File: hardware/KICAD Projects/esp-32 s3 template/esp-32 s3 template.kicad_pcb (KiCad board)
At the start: 2 copper layers, 55.5 x 39.5 mm, 28 parts, among them J1 TYPE-C-31-M-12, J2 TFTLCDS2, SW1 PTS810_SJM_250_SMTR_LFS, SW2 PTS810_SJM_250_SMTR_LFS, U1 AMS1117-3.3, U2 ESP32-S3-WROOM-1

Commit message: started the can integration
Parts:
- moved SW1 78.1 mm to (81.8, 71.6)
- moved SW2 77.8 mm to (81.8, 78.0)
- moved D6 76.4 mm to (79.6, 64.5), turned to 90 degrees
- moved C9 60.7 mm to (77.8, 71.7), turned to 90 degrees
- moved C10 59.5 mm to (77.7, 78.1), turned to 90 degrees
- moved R5 57.2 mm to (85.6, 71.5), turned to -90 degrees
- moved R4 56.7 mm to (87.0, 66.7), turned to 90 degrees
- moved C8 56.7 mm to (84.8, 63.1), turned to 90 degrees
- moved C6 56.7 mm to (84.8, 66.7), turned to -90 degrees
- moved R6 55.7 mm to (85.8, 77.9), turned to -90 degrees
- moved D3 54.5 mm to (110.2, 77.5)
- moved D2 54.4 mm to (110.3, 74.7)
- moved D4 54.4 mm to (110.2, 80.3)
- moved C7 53.6 mm to (87.0, 63.1), turned to 90 degrees
- moved D1 49.7 mm to (115.5, 70.0)
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
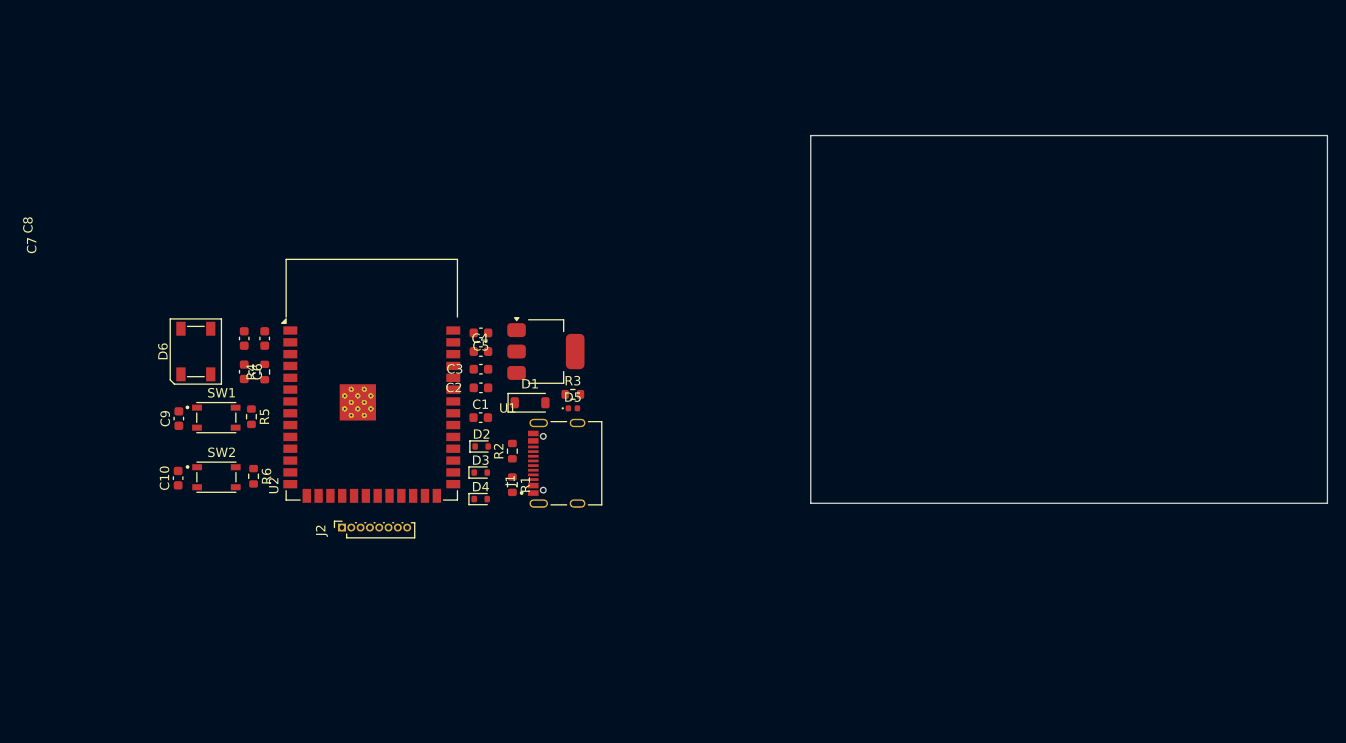
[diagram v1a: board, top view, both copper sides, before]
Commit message: finished pcb component layout for smd temp sense
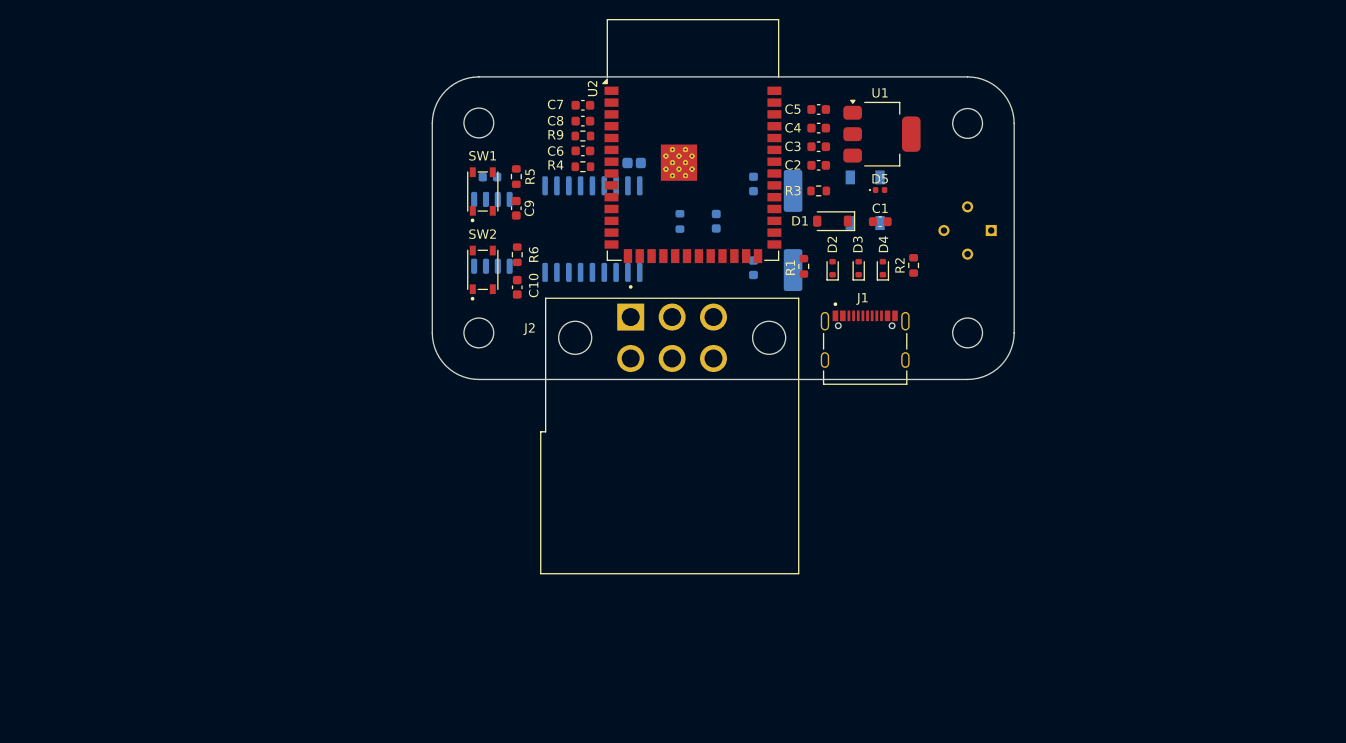
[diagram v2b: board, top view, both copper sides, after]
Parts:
- added C11: 10uF/16V, Capacitor_Tantalum_SMD:CP_EIA-1608-08_AVX-J, B.Cu at (126.7, 44.2)
- added C12: 100nF, Capacitor_SMD:C_0603_1608Metric, B.Cu at (135.5, 50.5)
- added C13: 22pF, Capacitor_SMD:C_0603_1608Metric, B.Cu at (139.5, 46.5)
- added C14: 22pF, Capacitor_SMD:C_0603_1608Metric, B.Cu at (139.5, 55.5)
- added C15: 100nF, Capacitor_SMD:C_0603_1608Metric, B.Cu at (111.2, 45.8)
- added R8: 10kΩ, Resistor_SMD:R_0603_1608Metric, B.Cu at (131.6, 50.5)
- added R9: 10k, Resistor_SMD:R_0603_1608Metric, F.Cu at (121.2, 41.4)
- added REF**: MountingHole_3.2mm_M3, MountingHole:MountingHole_3.2mm_M3, F.Cu at (110.0, 40.0)
- added REF**: MountingHole_3.2mm_M3, MountingHole:MountingHole_3.2mm_M3, F.Cu at (162.5, 62.5)
- added REF**: MountingHole_3.2mm_M3, MountingHole:MountingHole_3.2mm_M3, F.Cu at (162.5, 40.0)
- added REF**: MountingHole_3.2mm_M3, MountingHole:MountingHole_3.2mm_M3, F.Cu at (110.0, 62.5)
- added U3: MCP2515-I, Package_SO:SOIC-18W_7.5x11.6mm_P1.27mm, B.Cu at (122.2, 51.4)
- added U4: TJA1050DRG, Package_SO:SOIC-8_5.3x5.3mm_P1.27mm, B.Cu at (111.4, 51.8)
- added U5: ~, 0_Custom:MLX90614, B.Cu at (162.5, 51.5)
- added X1: 8MHz, Crystal:Crystal_SMD_HC49-SD, B.Cu at (143.8, 51.5)
- D6: moved to B.Cu
- J2: value TFTLCDS2 -> DTF13-6P; footprint Connector_PinSocket_1.00mm:PinSocket_1x08_P1.00mm_Vertical -> 0_Custom:TE_DTF13-6P
- moved D6 73.7 mm to (151.5, 48.2)
- moved D4 49.8 mm to (153.4, 55.5), turned to 90 degrees
- moved C1 47.8 mm to (153.1, 50.5)
- moved R2 47.5 mm to (156.7, 55.2)
- moved D3 46.2 mm to (150.8, 55.5), turned to 90 degrees
- moved C4 43.5 mm to (146.5, 40.5)
- moved C5 43.5 mm to (146.5, 38.5)
- moved C2 43.4 mm to (146.5, 44.5)
- moved C3 43.4 mm to (146.5, 42.5)
- moved C6 43.4 mm to (121.2, 43.0), turned to 180 degrees
- moved C8 43.2 mm to (121.2, 39.8), turned to 180 degrees
- moved U2 43.1 mm to (133.0, 41.8)
- moved U1 43.0 mm to (153.3, 41.1)
- moved C9 42.7 mm to (114.0, 49.1), turned to -90 degrees
- moved C7 42.4 mm to (121.2, 38.0), turned to 180 degrees
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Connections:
- C4 pad 1: ESP_3V3 -> VCC_3V3
- C5 pad 1: ESP_3V3 -> VCC_3V3
- C7 pad 1: ESP_3V3 -> VCC_3V3
- C8 pad 1: ESP_3V3 -> VCC_3V3
- D6 pad 3: ESP_3V3 -> VCC_3V3
- J2 pad 1: ESP_3V3 -> VCC_5V
- J2 pad 3: DIN -> Low
- J2 pad 4: CLK -> High
- J2 pad 5: CS -> Low
- J2 pad 6: DC -> High
- R3 pad 1: ESP_3V3 -> VCC_3V3
- R5 pad 1: ESP_3V3 -> VCC_3V3
- R6 pad 1: ESP_3V3 -> VCC_3V3
- U1 pad 2: ESP_3V3 -> VCC_3V3
- U2 pad 16: unconnected-(U2-IO46-Pad16) -> SCL
- U2 pad 2: ESP_3V3 -> VCC_3V3
- U2 pad 24: unconnected-(U2-IO47-Pad24) -> SO
- U2 pad 25: unconnected-(U2-IO48-Pad25) -> SI
- U2 pad 26: unconnected-(U2-IO45-Pad26) -> SDA
- U2 pad 38: unconnected-(U2-IO2-Pad38) -> VCC_3V3
- U2 pad 6: unconnected-(U2-IO6-Pad6) -> SCK
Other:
- board size 55.5 x 39.5 mm -> 62.5 x 32.5 mm

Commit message: everything but the ground fill
done, having some trouble with the ground fills
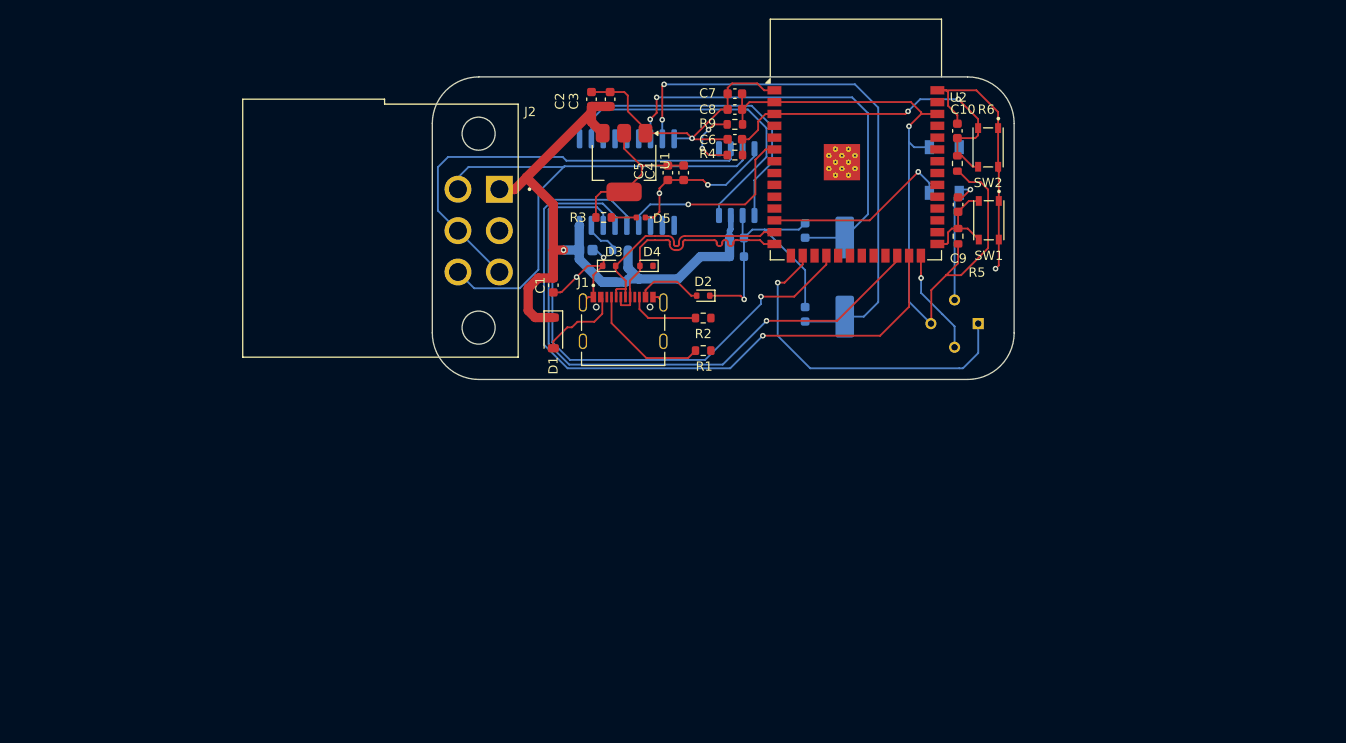
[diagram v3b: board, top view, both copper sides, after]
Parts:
- removed REF** (x4): MountingHole_3.2mm_M3, MountingHole:MountingHole_3.2mm_M3
- moved SW2 55.8 mm to (164.7, 42.6), turned to -90 degrees
- moved SW1 54.4 mm to (164.8, 50.4), turned to -90 degrees
- moved C10 50.2 mm to (161.4, 40.8), turned to 90 degrees
- moved R6 48.3 mm to (161.4, 44.3)
- moved R5 47.9 mm to (161.5, 52.1)
- moved C9 47.5 mm to (161.5, 48.7), turned to 90 degrees
- moved C1 35.8 mm to (118.0, 57.4), turned to -90 degrees
- moved D1 32.3 mm to (118.0, 62.5), turned to -90 degrees
- moved U1 27.9 mm to (125.6, 44.2), turned to -90 degrees
- moved C15 27.3 mm to (137.7, 52.3), turned to 180 degrees
- moved U4 26.9 mm to (137.7, 46.3), turned to 90 degrees
- moved D3 26.8 mm to (124.0, 55.3), turned to 0 degrees
- moved J1 26.1 mm to (125.5, 63.4)
- moved D5 25.9 mm to (127.4, 50.1), turned to 180 degrees
- moved C2 25.4 mm to (122.1, 37.4), turned to 90 degrees
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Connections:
- U2 pad 12: DIN -> RGB
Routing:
- net GND: track 0.00 -> 140.1 mm, vias 0 -> 8
- net VCC_3V3: track 0.00 -> 95.5 mm, vias 0 -> 1
- net VCC_5V: track 0.00 -> 74.3 mm, vias 0 -> 1
- net SI: track 0.00 -> 74.1 mm, vias 0 -> 1
- net SO: track 0.00 -> 66.9 mm, vias 0 -> 1
- net Net-(U3-OSC1): track 0.00 -> 59.6 mm, vias 0 -> 2
- net CS: track 0.00 -> 57.2 mm, vias 0 -> 1
- net High: track 0.00 -> 56.3 mm
- net Low: track 0.00 -> 47.3 mm
- net Net-(U3-OSC2): track 0.00 -> 46.8 mm, vias 0 -> 2
- net CHIP_PU: track 0.00 -> 39.0 mm, vias 0 -> 2
- net SCL: track 0.00 -> 37.0 mm, vias 0 -> 1
- net Net-(U3-TXCAN): track 0.00 -> 34.7 mm
- net Net-(U3-RXCAN): track 0.00 -> 33.6 mm
- net D+: track 0.00 -> 26.3 mm
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
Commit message: Finished it
Figured out zone fills
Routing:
- added copper zone on B.Cu, net GND
- added copper zone on F.Cu, net GND
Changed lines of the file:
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@@
 		(net 58)
+	)
+	(zone
+		(net 2)
+		(net_name "GND")
+		(layers "F.Cu" "B.Cu")
+		(hatch edge 0.5)
+		(connect_pads
+			(clearance 0.5)
+		)
+		(min_thickness 0.25)
+		(filled_areas_thickness no)
+		(fill yes
+			(thermal_gap 0.5)
+			(thermal_bridge_width 0.5)
+		)
+		(polygon
+			(pts
+				(xy 110 35) (xy 105 40) (xy 105 63) (xy 110 67.5) (xy 162 67.5) (xy 167.5 62) (xy 167.5 40) (xy 162 35)
+			)
+		)
 	)
 	(generated

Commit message: nfkljasdnfl
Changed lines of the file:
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@@
 			(outputformat 1)
 			(mirror no)
-			(drillshape 1)
+			(drillshape 0)
 			(scaleselection 1)
-			(outputdirectory "")
+			(outputdirectory "Gerbers/")
 		)
 	)
@@
 		(tags "CMS SOT")
 		(property "Reference" "U1"
-			(at -0.2 -4.4 90)
+			(at -1.9 -5.2 90)
 			(layer "F.SilkS")
 			(effects
